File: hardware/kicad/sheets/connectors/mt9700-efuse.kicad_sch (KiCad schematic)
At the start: 8 parts

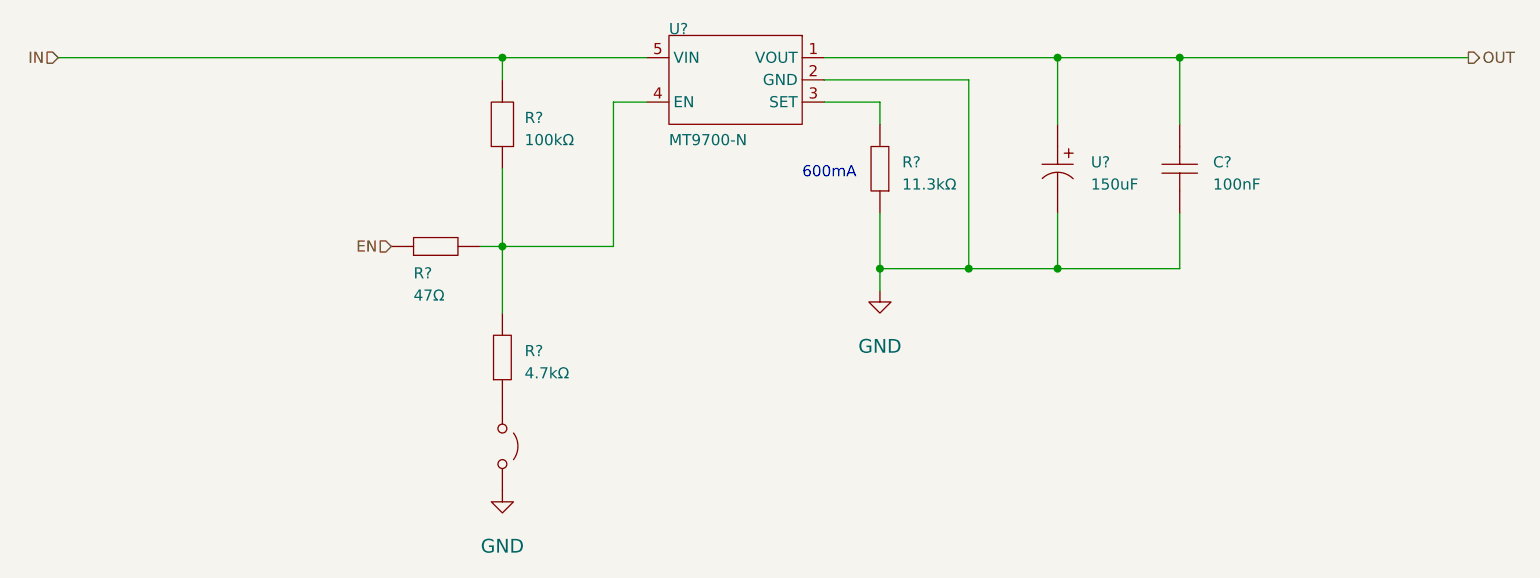
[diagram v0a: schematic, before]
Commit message: resheeted bms and fixed links for the 12v buck
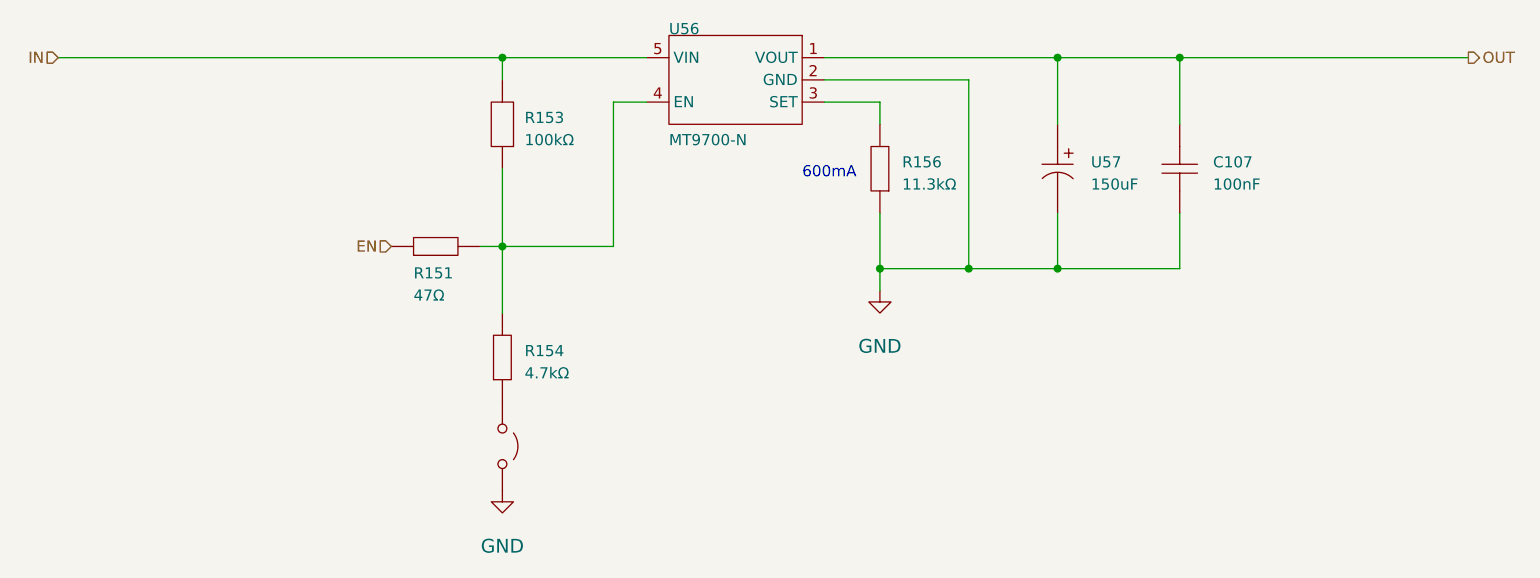
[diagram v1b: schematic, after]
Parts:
- gave numbers to parts that had none: 8
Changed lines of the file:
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@@
 		(on_board yes)
 		(dnp no)
-		(property "Reference" "#PWR074"
+		(property "Reference" "#PWR0158"
 			(at 160.02 102.87 0)
 			(effects
@@
 			(project "svea_powerboard_rev3"
 				(path "/3f85abf4-0b95-4c4a-b7e9-06f59ca1ea3d/5c2e021f-c2d4-49e2-8c36-9a64f1f12005/8d05c3b8-20a4-4a7f-9b20-01f8d5d5be51/1ab26688-c62b-4751-9925-b75256f43ad8"
-					(reference "#PWR074")
+					(reference "#PWR0158")
 					(unit 1)
 				)
@@
 		(on_board yes)
 		(dnp no)
-		(property "Reference" "R?"
+		(property "Reference" "R151"
 			(at 106.68 101.6 0)
 			(effects
@@
 			(project "svea_powerboard_rev3"
 				(path "/3f85abf4-0b95-4c4a-b7e9-06f59ca1ea3d/5c2e021f-c2d4-49e2-8c36-9a64f1f12005/8d05c3b8-20a4-4a7f-9b20-01f8d5d5be51/1ab26688-c62b-4751-9925-b75256f43ad8"
-					(reference "R?")
+					(reference "R151")
 					(unit 1)
 				)
@@
 		(on_board yes)
 		(dnp no)
-		(property "Reference" "U?"
+		(property "Reference" "U57"
 			(at 184.15 88.9 90)
 			(effects
@@
 			(project "svea_powerboard_rev3"
 				(path "/3f85abf4-0b95-4c4a-b7e9-06f59ca1ea3d/5c2e021f-c2d4-49e2-8c36-9a64f1f12005/8d05c3b8-20a4-4a7f-9b20-01f8d5d5be51/1ab26688-c62b-4751-9925-b75256f43ad8"
-					(reference "U?")
+					(reference "U57")
 					(unit 1)
 				)
@@
 		(on_board yes)
 		(dnp no)
-		(property "Reference" "#PWR073"
+		(property "Reference" "#PWR0156"
 			(at 116.84 125.73 0)
 			(effects
@@
 			(project "svea_powerboard_rev3"
 				(path "/3f85abf4-0b95-4c4a-b7e9-06f59ca1ea3d/5c2e021f-c2d4-49e2-8c36-9a64f1f12005/8d05c3b8-20a4-4a7f-9b20-01f8d5d5be51/1ab26688-c62b-4751-9925-b75256f43ad8"
-					(reference "#PWR073")
+					(reference "#PWR0156")
 					(unit 1)
 				)
@@
 		(on_board yes)
 		(dnp no)
-		(property "Reference" "U?"
+		(property "Reference" "U55"
 			(at 119.38 120.65 90)
 			(effects
@@
 			(project "svea_powerboard_rev3"
 				(path "/3f85abf4-0b95-4c4a-b7e9-06f59ca1ea3d/5c2e021f-c2d4-49e2-8c36-9a64f1f12005/8d05c3b8-20a4-4a7f-9b20-01f8d5d5be51/1ab26688-c62b-4751-9925-b75256f43ad8"
-					(reference "U?")
+					(reference "U55")
 					(unit 1)
 				)
@@
 		(on_board yes)
 		(dnp no)
-		(property "Reference" "C?"
+		(property "Reference" "C107"
 			(at 198.12 88.9 90)
 			(effects
@@
 			(project "svea_powerboard_rev3"
 				(path "/3f85abf4-0b95-4c4a-b7e9-06f59ca1ea3d/5c2e021f-c2d4-49e2-8c36-9a64f1f12005/8d05c3b8-20a4-4a7f-9b20-01f8d5d5be51/1ab26688-c62b-4751-9925-b75256f43ad8"
-					(reference "C?")
+					(reference "C107")
 					(unit 1)
 				)
@@
 		(on_board yes)
 		(dnp no)
-		(property "Reference" "R?"
+		(property "Reference" "R154"
 			(at 119.38 110.49 90)
 			(effects
@@
 			(project "svea_powerboard_rev3"
 				(path "/3f85abf4-0b95-4c4a-b7e9-06f59ca1ea3d/5c2e021f-c2d4-49e2-8c36-9a64f1f12005/8d05c3b8-20a4-4a7f-9b20-01f8d5d5be51/1ab26688-c62b-4751-9925-b75256f43ad8"
-					(reference "R?")
+					(reference "R154")
 					(unit 1)
 				)
@@
 		(on_board yes)
 		(dnp no)
-		(property "Reference" "R?"
+		(property "Reference" "R153"
 			(at 119.38 83.82 90)
 			(effects
@@
 			(project "svea_powerboard_rev3"
 				(path "/3f85abf4-0b95-4c4a-b7e9-06f59ca1ea3d/5c2e021f-c2d4-49e2-8c36-9a64f1f12005/8d05c3b8-20a4-4a7f-9b20-01f8d5d5be51/1ab26688-c62b-4751-9925-b75256f43ad8"
-					(reference "R?")
+					(reference "R153")
 					(unit 1)
 				)
@@
 		(on_board yes)
 		(dnp no)
-		(property "Reference" "U?"
+		(property "Reference" "U56"
 			(at 135.89 73.66 0)
 			(effects
@@
 			(project "svea_powerboard_rev3"
 				(path "/3f85abf4-0b95-4c4a-b7e9-06f59ca1ea3d/5c2e021f-c2d4-49e2-8c36-9a64f1f12005/8d05c3b8-20a4-4a7f-9b20-01f8d5d5be51/1ab26688-c62b-4751-9925-b75256f43ad8"
-					(reference "U?")
+					(reference "U56")
 					(unit 1)
 				)
@@
 		(on_board yes)
 		(dnp no)
-		(property "Reference" "R?"
+		(property "Reference" "R156"
 			(at 162.56 88.9 90)
 			(effects
@@
 			(project "svea_powerboard_rev3"
 				(path "/3f85abf4-0b95-4c4a-b7e9-06f59ca1ea3d/5c2e021f-c2d4-49e2-8c36-9a64f1f12005/8d05c3b8-20a4-4a7f-9b20-01f8d5d5be51/1ab26688-c62b-4751-9925-b75256f43ad8"
-					(reference "R?")
+					(reference "R156")
 					(unit 1)
 				)

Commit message: starting transition to single root
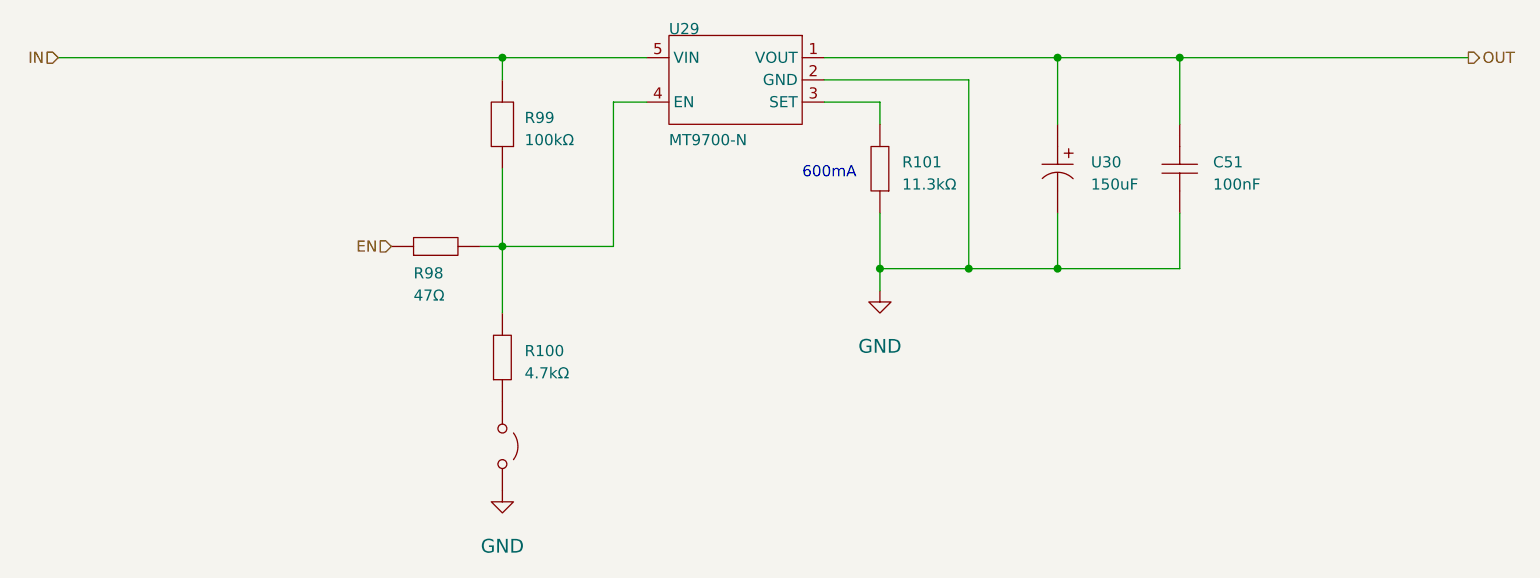
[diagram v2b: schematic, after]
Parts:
- renumbered C107 to C51, R154 to R100, R156 to R101, R151 to R98, R153 to R99, U55 to U28, U56 to U29, U57 to U30
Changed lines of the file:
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@@
 		(on_board yes)
 		(dnp no)
-		(property "Reference" "#PWR0158"
+		(property "Reference" "#PWR092"
 			(at 160.02 102.87 0)
 			(effects
@@
 		(instances
 			(project "svea_powerboard_rev3"
-				(path "/3f85abf4-0b95-4c4a-b7e9-06f59ca1ea3d/5c2e021f-c2d4-49e2-8c36-9a64f1f12005/8d05c3b8-20a4-4a7f-9b20-01f8d5d5be51/1ab26688-c62b-4751-9925-b75256f43ad8"
-					(reference "#PWR0158")
+				(path "/3f85abf4-0b95-4c4a-b7e9-06f59ca1ea3d/5c2e021f-c2d4-49e2-8c36-9a64f1f12001/1d4a251e-4375-4aab-85e0-d11dfb5595c0"
+					(reference "#PWR092")
 					(unit 1)
 				)
@@
 		(on_board yes)
 		(dnp no)
-		(property "Reference" "R151"
+		(property "Reference" "R98"
 			(at 106.68 101.6 0)
 			(effects
@@
 		(instances
 			(project "svea_powerboard_rev3"
-				(path "/3f85abf4-0b95-4c4a-b7e9-06f59ca1ea3d/5c2e021f-c2d4-49e2-8c36-9a64f1f12005/8d05c3b8-20a4-4a7f-9b20-01f8d5d5be51/1ab26688-c62b-4751-9925-b75256f43ad8"
-					(reference "R151")
+				(path "/3f85abf4-0b95-4c4a-b7e9-06f59ca1ea3d/5c2e021f-c2d4-49e2-8c36-9a64f1f12001/1d4a251e-4375-4aab-85e0-d11dfb5595c0"
+					(reference "R98")
 					(unit 1)
 				)
@@
 		(on_board yes)
 		(dnp no)
-		(property "Reference" "U57"
+		(property "Reference" "U30"
 			(at 184.15 88.9 90)
 			(effects
@@
 		(instances
 			(project "svea_powerboard_rev3"
-				(path "/3f85abf4-0b95-4c4a-b7e9-06f59ca1ea3d/5c2e021f-c2d4-49e2-8c36-9a64f1f12005/8d05c3b8-20a4-4a7f-9b20-01f8d5d5be51/1ab26688-c62b-4751-9925-b75256f43ad8"
-					(reference "U57")
+				(path "/3f85abf4-0b95-4c4a-b7e9-06f59ca1ea3d/5c2e021f-c2d4-49e2-8c36-9a64f1f12001/1d4a251e-4375-4aab-85e0-d11dfb5595c0"
+					(reference "U30")
 					(unit 1)
 				)
@@
 		(on_board yes)
 		(dnp no)
-		(property "Reference" "#PWR0156"
+		(property "Reference" "#PWR088"
 			(at 116.84 125.73 0)
 			(effects
@@
 		(instances
 			(project "svea_powerboard_rev3"
-				(path "/3f85abf4-0b95-4c4a-b7e9-06f59ca1ea3d/5c2e021f-c2d4-49e2-8c36-9a64f1f12005/8d05c3b8-20a4-4a7f-9b20-01f8d5d5be51/1ab26688-c62b-4751-9925-b75256f43ad8"
-					(reference "#PWR0156")
+				(path "/3f85abf4-0b95-4c4a-b7e9-06f59ca1ea3d/5c2e021f-c2d4-49e2-8c36-9a64f1f12001/1d4a251e-4375-4aab-85e0-d11dfb5595c0"
+					(reference "#PWR088")
 					(unit 1)
 				)
@@
 		(on_board yes)
 		(dnp no)
-		(property "Reference" "U55"
+		(property "Reference" "U28"
 			(at 119.38 120.65 90)
 			(effects
@@
 		(instances
 			(project "svea_powerboard_rev3"
-				(path "/3f85abf4-0b95-4c4a-b7e9-06f59ca1ea3d/5c2e021f-c2d4-49e2-8c36-9a64f1f12005/8d05c3b8-20a4-4a7f-9b20-01f8d5d5be51/1ab26688-c62b-4751-9925-b75256f43ad8"
-					(reference "U55")
+				(path "/3f85abf4-0b95-4c4a-b7e9-06f59ca1ea3d/5c2e021f-c2d4-49e2-8c36-9a64f1f12001/1d4a251e-4375-4aab-85e0-d11dfb5595c0"
+					(reference "U28")
 					(unit 1)
 				)
@@
 		(on_board yes)
 		(dnp no)
-		(property "Reference" "C107"
+		(property "Reference" "C51"
 			(at 198.12 88.9 90)
 			(effects
@@
 		(instances
 			(project "svea_powerboard_rev3"
-				(path "/3f85abf4-0b95-4c4a-b7e9-06f59ca1ea3d/5c2e021f-c2d4-49e2-8c36-9a64f1f12005/8d05c3b8-20a4-4a7f-9b20-01f8d5d5be51/1ab26688-c62b-4751-9925-b75256f43ad8"
-					(reference "C107")
+				(path "/3f85abf4-0b95-4c4a-b7e9-06f59ca1ea3d/5c2e021f-c2d4-49e2-8c36-9a64f1f12001/1d4a251e-4375-4aab-85e0-d11dfb5595c0"
+					(reference "C51")
 					(unit 1)
 				)
@@
 		(on_board yes)
 		(dnp no)
-		(property "Reference" "R154"
+		(property "Reference" "R100"
 			(at 119.38 110.49 90)
 			(effects
@@
 		(instances
 			(project "svea_powerboard_rev3"
-				(path "/3f85abf4-0b95-4c4a-b7e9-06f59ca1ea3d/5c2e021f-c2d4-49e2-8c36-9a64f1f12005/8d05c3b8-20a4-4a7f-9b20-01f8d5d5be51/1ab26688-c62b-4751-9925-b75256f43ad8"
-					(reference "R154")
+				(path "/3f85abf4-0b95-4c4a-b7e9-06f59ca1ea3d/5c2e021f-c2d4-49e2-8c36-9a64f1f12001/1d4a251e-4375-4aab-85e0-d11dfb5595c0"
+					(reference "R100")
 					(unit 1)
 				)
@@
 		(on_board yes)
 		(dnp no)
-		(property "Reference" "R153"
+		(property "Reference" "R99"
 			(at 119.38 83.82 90)
 			(effects
@@
 		(instances
 			(project "svea_powerboard_rev3"
-				(path "/3f85abf4-0b95-4c4a-b7e9-06f59ca1ea3d/5c2e021f-c2d4-49e2-8c36-9a64f1f12005/8d05c3b8-20a4-4a7f-9b20-01f8d5d5be51/1ab26688-c62b-4751-9925-b75256f43ad8"
-					(reference "R153")
+				(path "/3f85abf4-0b95-4c4a-b7e9-06f59ca1ea3d/5c2e021f-c2d4-49e2-8c36-9a64f1f12001/1d4a251e-4375-4aab-85e0-d11dfb5595c0"
+					(reference "R99")
 					(unit 1)
 				)
@@
 		(on_board yes)
 		(dnp no)
-		(property "Reference" "U56"
+		(property "Reference" "U29"
 			(at 135.89 73.66 0)
 			(effects
@@
 		(instances
 			(project "svea_powerboard_rev3"
-				(path "/3f85abf4-0b95-4c4a-b7e9-06f59ca1ea3d/5c2e021f-c2d4-49e2-8c36-9a64f1f12005/8d05c3b8-20a4-4a7f-9b20-01f8d5d5be51/1ab26688-c62b-4751-9925-b75256f43ad8"
-					(reference "U56")
+				(path "/3f85abf4-0b95-4c4a-b7e9-06f59ca1ea3d/5c2e021f-c2d4-49e2-8c36-9a64f1f12001/1d4a251e-4375-4aab-85e0-d11dfb5595c0"
+					(reference "U29")
 					(unit 1)
 				)
@@
 		(on_board yes)
 		(dnp no)
-		(property "Reference" "R156"
+		(property "Reference" "R101"
 			(at 162.56 88.9 90)
 			(effects
@@
 		(instances
 			(project "svea_powerboard_rev3"
-				(path "/3f85abf4-0b95-4c4a-b7e9-06f59ca1ea3d/5c2e021f-c2d4-49e2-8c36-9a64f1f12005/8d05c3b8-20a4-4a7f-9b20-01f8d5d5be51/1ab26688-c62b-4751-9925-b75256f43ad8"
-					(reference "R156")
+				(path "/3f85abf4-0b95-4c4a-b7e9-06f59ca1ea3d/5c2e021f-c2d4-49e2-8c36-9a64f1f12001/1d4a251e-4375-4aab-85e0-d11dfb5595c0"
+					(reference "R101")
 					(unit 1)
 				)

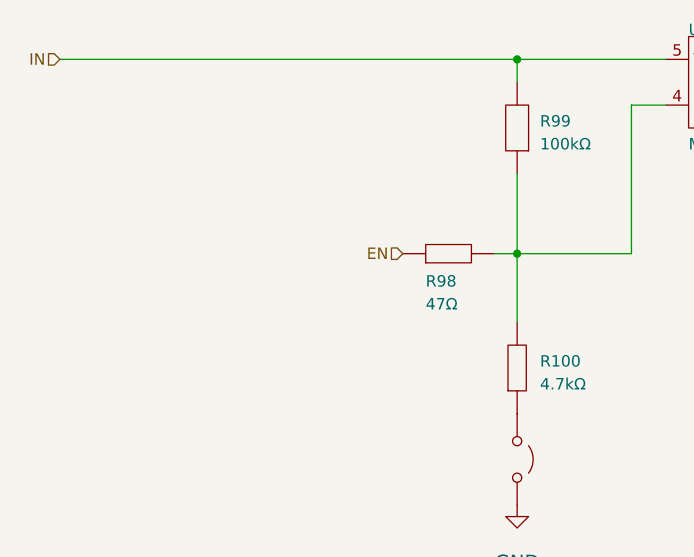
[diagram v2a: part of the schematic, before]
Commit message: realized having 2 3v3 rails can cause issues
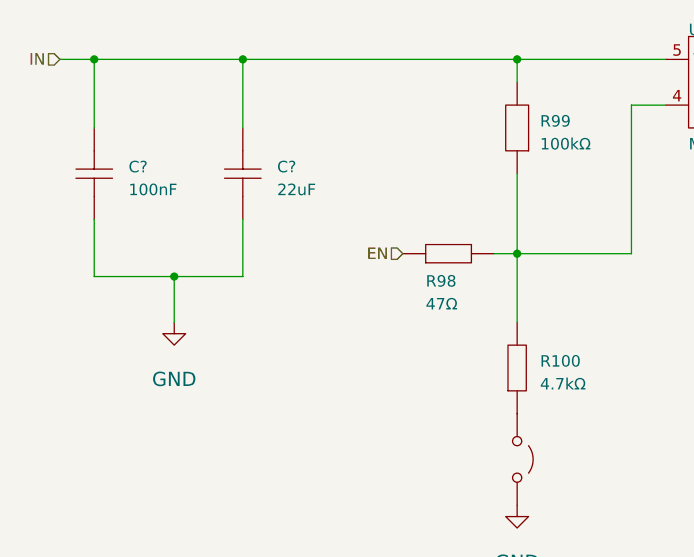
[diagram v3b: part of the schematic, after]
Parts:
- added C?: 100nF, Capacitor_SMD:C_0603_1608Metric, symbol 5v rail sm-easyedapro:CC0603KRX7R9BB104
- added C?: 22uF, Capacitor_SMD:C_0603_1608Metric, symbol 5v rail sm-easyedapro:CL10A226MP8NUNE
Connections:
- net GND: now also C?.1, C?.1
- net IN: now also C?.2, C?.2
